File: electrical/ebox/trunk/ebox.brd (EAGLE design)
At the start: 100 x 80 mm, 162 parts, among them IC1 MAX3221CUE, IC10 SN74LVC1G125, IC11 MAX3221CUE, IC12 INA170, IC13 SN74LVC1G125, IC14 SN74LVC1G125, IC15 MAX3221CUE, IC17 SN74LVC1G125, IC18 SN74LVC1G125, IC19 74ALS04D, IC2 LT3652, IC20 AP1509-33, IC24 AP1509-5, IC3 XMEGA128A1, IC4 LT1161, IC5 SN74LVC1G125, IC6 SN74LVC1G125, IC7 MAX3221CUE, IC8 INA170, IC9 SN74LVC1G125, Q1 FDD4141TO252, U1 BLUETOOTH-RN42, U2 D2523T_, X1 BULLET, X10 DEANS, X11 DEANS, X12 7381-2PG-300, X13 B4B-ZR, X14 BULLET, X17 22-23-2021, X18 7381-3PG-300, X19 7381-3PG-300, X2 BULLET, X20 BULLET, X21 BULLET, X22 BULLET, X23 BULLET, X24 B4B-ZR, X3 17984-7PG-300, X4 BULLET, X5 17984-7PG-300, X6 17984-7PG-300, X7 17984-7PG-300, X8 22-23-2031, X9 22-23-2031

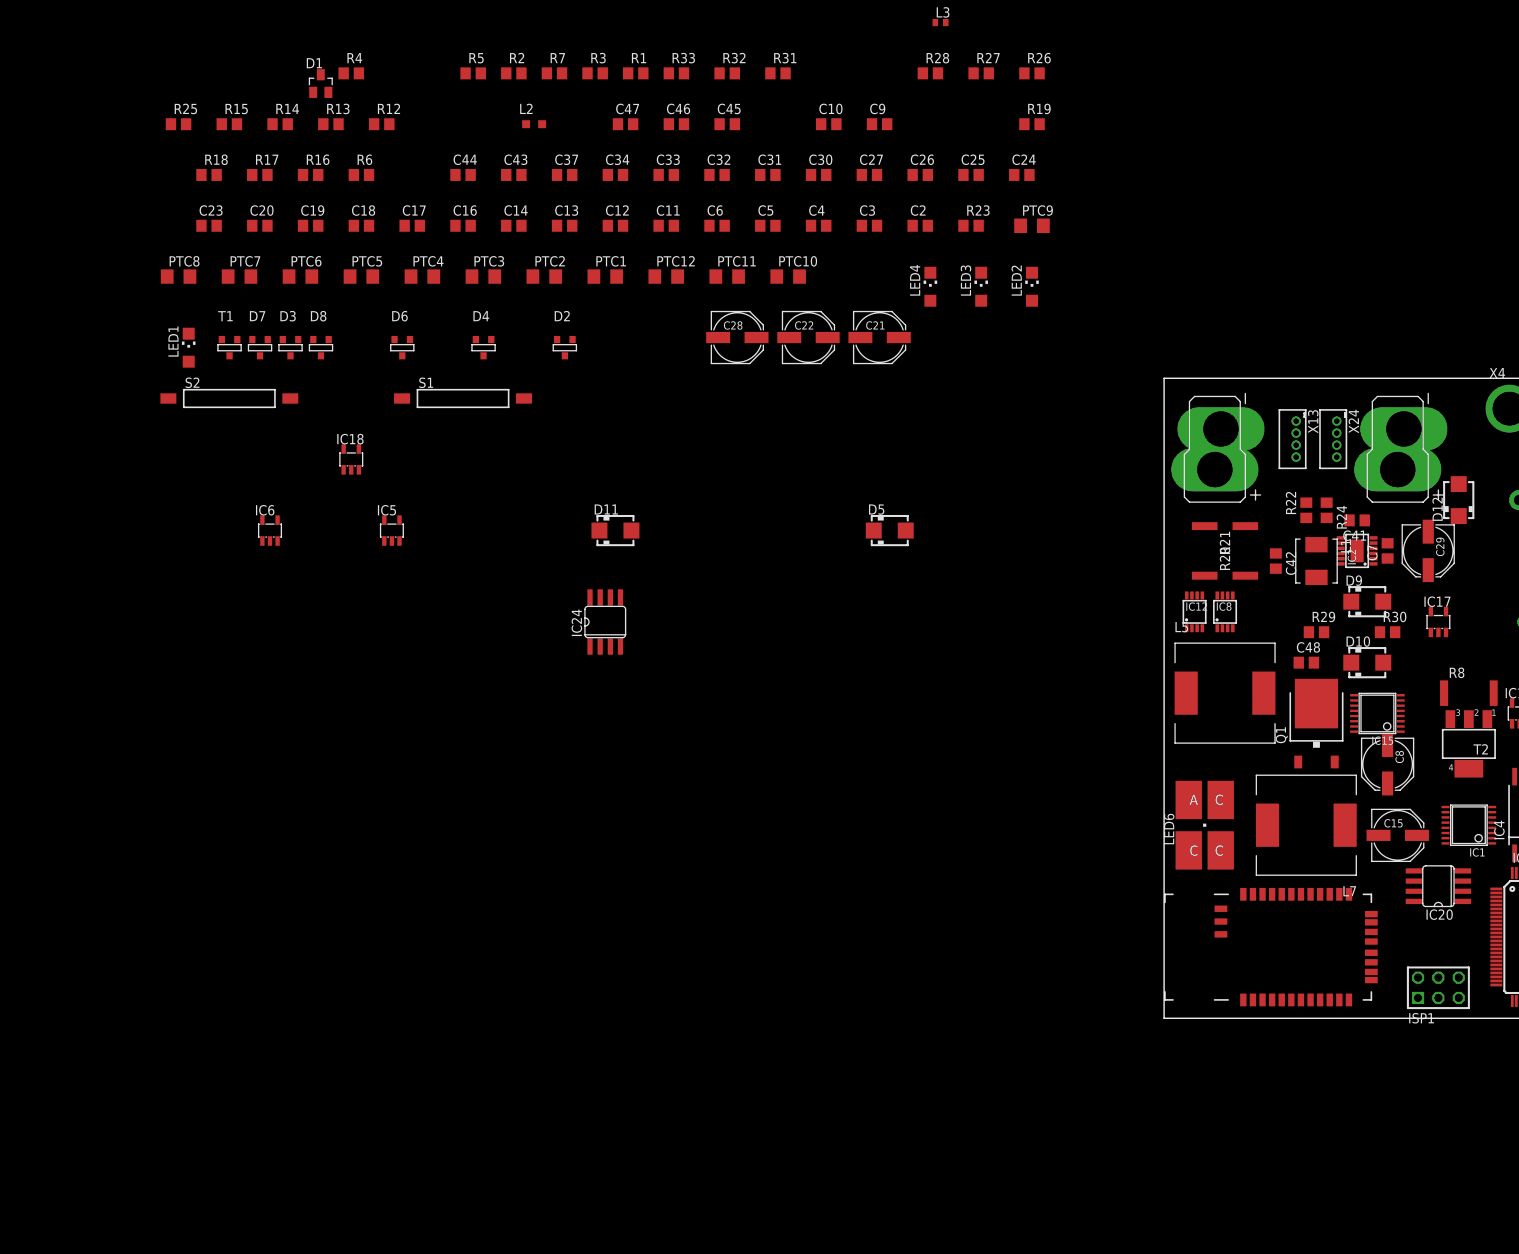
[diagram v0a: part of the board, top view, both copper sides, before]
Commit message: Removed switching regulators, replaced with onboard ESC BEC power.
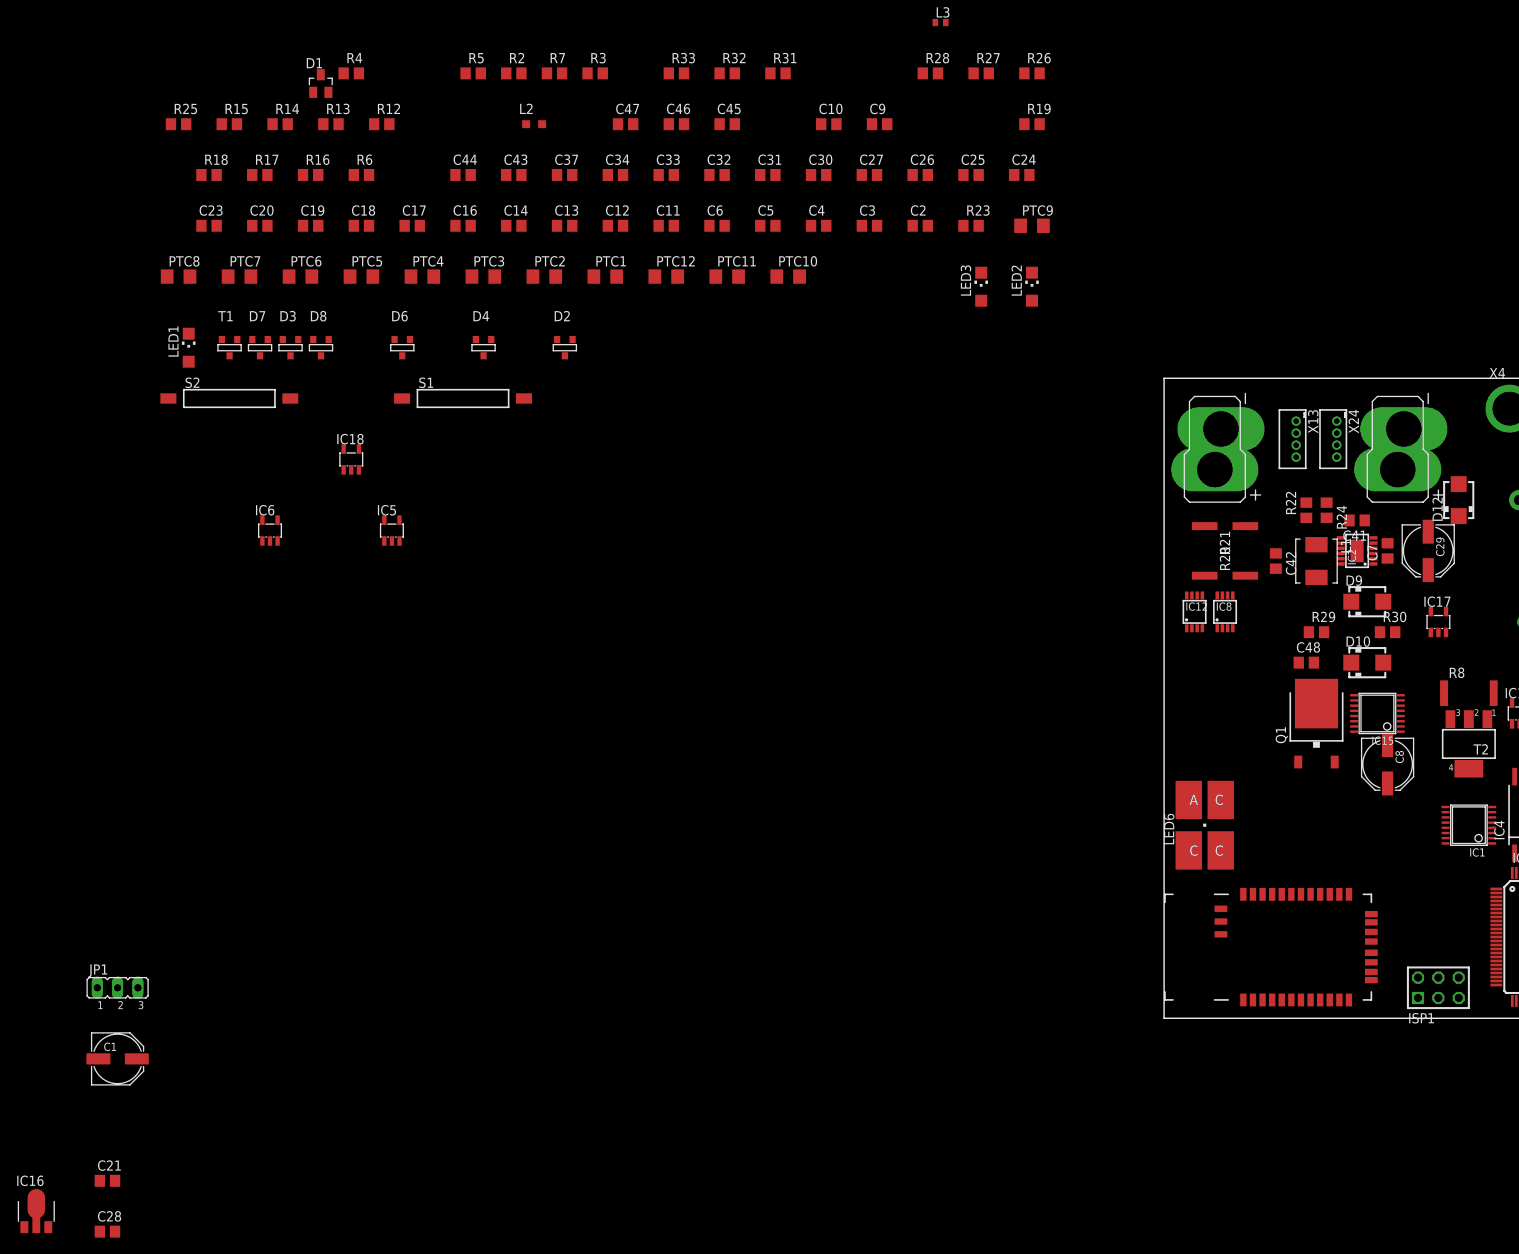
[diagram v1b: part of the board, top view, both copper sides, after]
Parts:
- removed C15: 68uF, rcl:PANASONIC_D
- removed C22: 220uF, rcl:PANASONIC_D
- removed D11, D5: MBRA340T3, diode:SMA
- removed IC20: AP1509-33, crw:SO08
- removed IC24: AP1509-5, crw:SO08
- removed L5, L7: 47uH, crw:SRR1280
- removed LED4: RED, led:CHIPLED_1206
- removed R1: 330, rcl:R0805
- added C1: 68uF, rcl:PANASONIC_D
- added IC16: MCP170333MB, linear:SOT89
- added JP1: (no value), jumper:JP2
- C21: value 68uF -> 1uF; device rcl:PANASONIC_D -> rcl:C0805
- C28: value 220uF -> 1uF; device rcl:PANASONIC_D -> rcl:C0805
- moved C21 142.9 mm to (-132.1, -20.3)
- moved C28 136.7 mm to (-132.1, -26.7)
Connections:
- removed net N$40: D5.C, IC20.2, L7.1
- removed net N$45: D11.C, IC24.2, L5.1
- removed net N$46: LED4.A, R1.1
- new net MOT1_5V: JP1.3, X8.2
- new net MOT2_5V: JP1.1, X9.2
- net +12V: no longer C15.+, C21.+, IC20.1, IC24.1
- net +3V3: now also C28.1, IC16.3; no longer C22.+, IC20.3, L7.2, R1.2
- net +5V: now also C1.+, C21.1, IC16.2@1, JP1.2; no longer C28.+, IC24.3, L5.2
- net GND: now also C1.-, C21.2, C28.2, IC16.1; no longer C15.-, C21.-, C22.-, C28.-, D11.A, D5.A, IC20.4, IC20.5, IC20.6, IC20.7, IC20.8, IC24.4, IC24.5, IC24.6, IC24.7, IC24.8, LED4.C

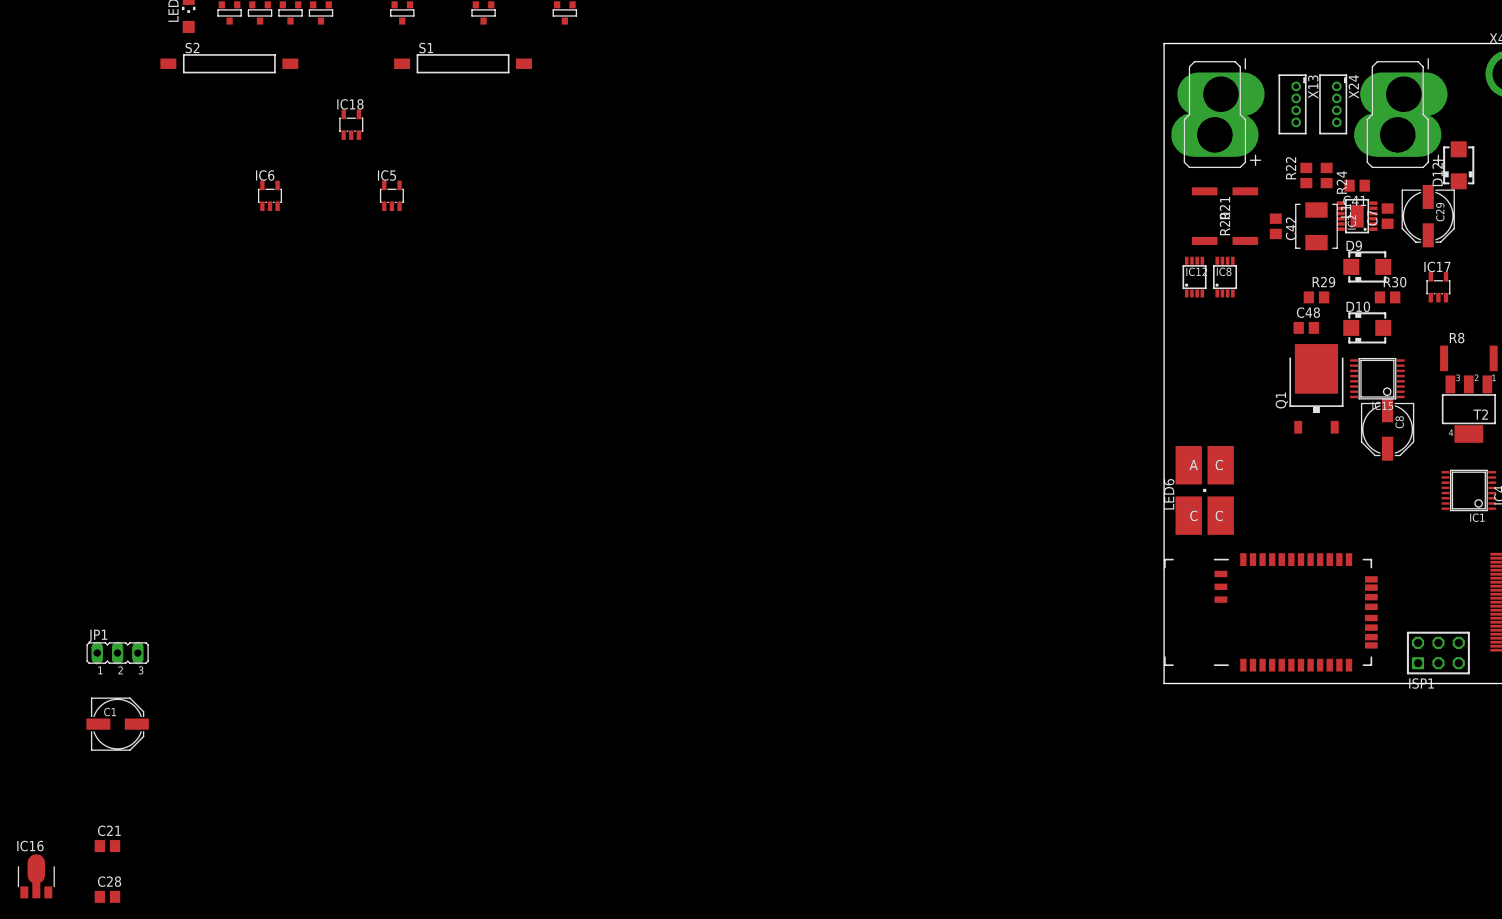
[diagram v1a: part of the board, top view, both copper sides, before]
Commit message: Added missing battery connectors for ESC.
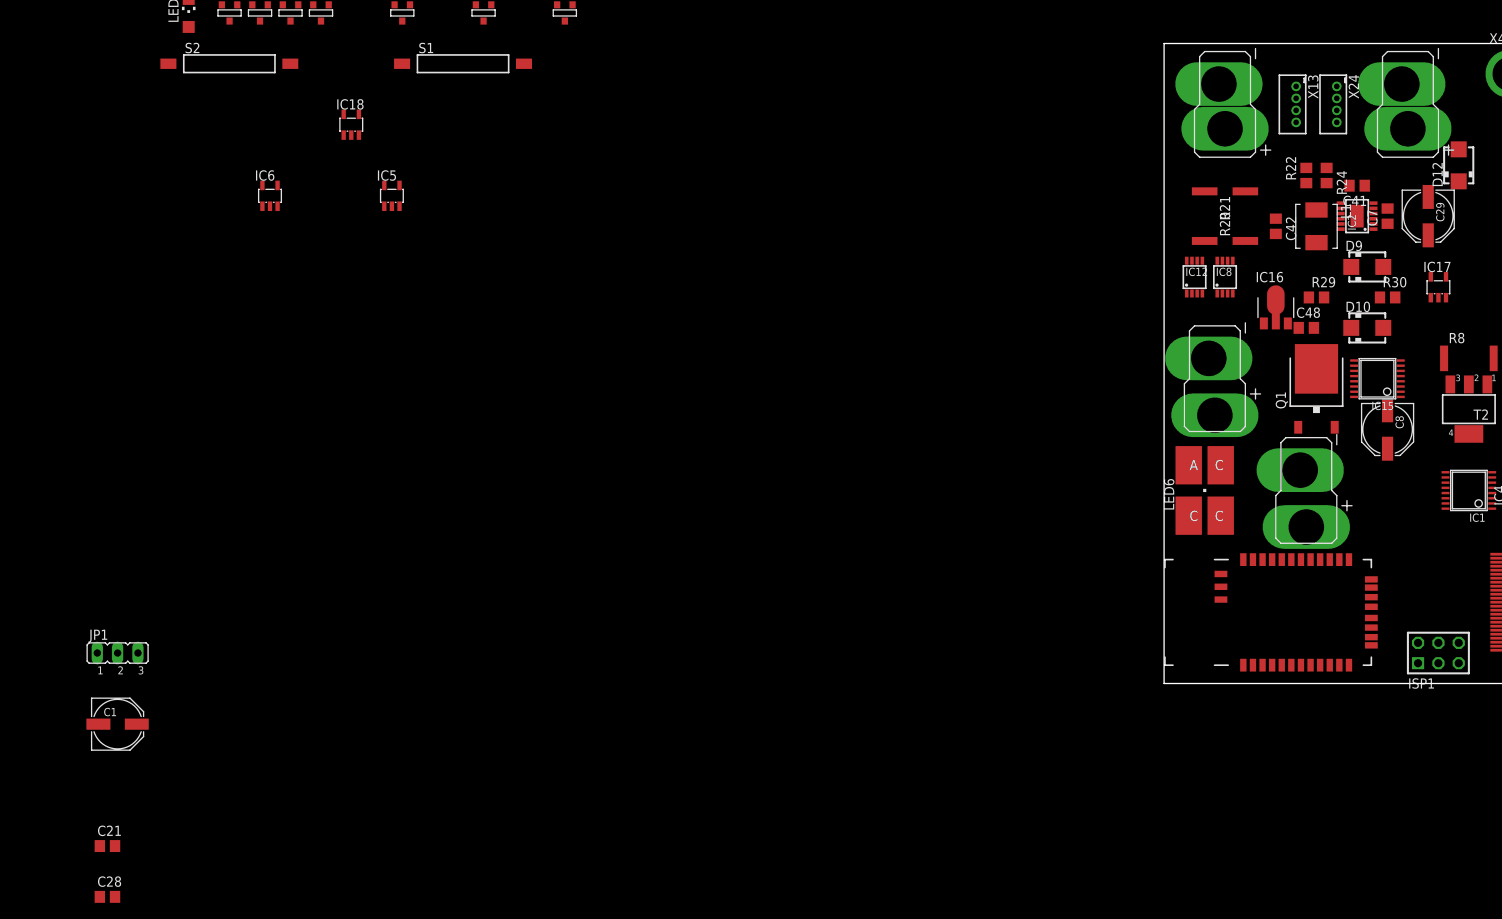
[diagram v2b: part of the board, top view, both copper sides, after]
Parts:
- added X15, X16: DEANS-FEMALE, crw:DEANS_FEMALE
- X10, X11: value DEANS -> DEANS-MALE; device crw:DEANS -> crw:DEANS_MALE
- moved IC16 170.5 mm to (14.0, 47.0)
- moved X10 1.80 mm to (7.62, 72.4)
- moved X11 1.80 mm to (30.5, 72.4)
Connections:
- net +12V: now also X15.POS, X16.POS
- net GND: now also X15.NEG, X16.NEG
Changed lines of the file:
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@@
 <element name="R32" library="rcl" package="R0805" value="330" x="-54.61" y="118.11"/>
 <element name="R33" library="rcl" package="R0805" value="330" x="-60.96" y="118.11"/>
-<element name="X10" library="crw" package="DEANS" value="DEANS" x="6.35" y="71.12"/>
-<element name="X11" library="crw" package="DEANS" value="DEANS" x="29.21" y="71.12"/>
 <element name="X12" library="crw" package="7381-2PG-300" value="7381-2PG-300" x="46.99" y="64.77" rot="MR0"/>
 <element name="X3" library="crw" package="17984-7PG-300" value="17984-7PG-300" x="46.99" y="49.53" rot="MR0"/>
@@
 <element name="C21" library="rcl" package="C0805" value="1uF" x="-132.08" y="-20.32"/>
 <element name="C28" library="rcl" package="C0805" value="1uF" x="-132.08" y="-26.67"/>
-<element name="IC16" library="linear" package="SOT89" value="MCP170333MB" x="-140.97" y="-24.13"/>
+<element name="IC16" library="linear" package="SOT89" value="MCP170333MB" x="13.97" y="46.99"/>
+<element name="X15" library="crw" package="DEANS_FEMALE" value="DEANS-FEMALE" x="6.35" y="38.1"/>
+<element name="X16" library="crw" package="DEANS_FEMALE" value="DEANS-FEMALE" x="17.78" y="24.13"/>
+<element name="X10" library="crw" package="DEANS_MALE" value="DEANS-MALE" x="7.62" y="72.39"/>
+<element name="X11" library="crw" package="DEANS_MALE" value="DEANS-MALE" x="30.48" y="72.39"/>
 </elements>
 <signals>
@@
 <contactref element="C21" pad="2"/>
 <contactref element="IC16" pad="1"/>
-<wire x1="-131.13" y1="-26.67" x2="-142.469" y2="-26.111" width="0" layer="19" extent="1-1"/>
+<contactref element="X15" pad="NEG"/>
+<contactref element="X16" pad="NEG"/>
+<wire x1="5.588" y1="40.64" x2="17.018" y2="26.67" width="0" layer="19" extent="1-1"/>
+<wire x1="12.471" y1="45.009" x2="5.588" y2="40.64" width="0" layer="19" extent="1-1"/>
+<wire x1="-131.13" y1="-26.67" x2="12.471" y2="45.009" width="0" layer="19" extent="1-1"/>
 <wire x1="-131.13" y1="-20.32" x2="-131.13" y2="-26.67" width="0" layer="19" extent="1-1"/>
 <wire x1="-133.21" y1="-5.08" x2="-131.13" y2="-20.32" width="0" layer="19" extent="1-1"/>
@@
 <contactref element="C28" pad="1"/>
 <contactref element="IC16" pad="3"/>
-<wire x1="-133.03" y1="-26.67" x2="-139.471" y2="-26.111" width="0" layer="19" extent="1-1"/>
+<wire x1="-133.03" y1="-26.67" x2="15.469" y2="45.009" width="0" layer="19" extent="1-1"/>
 <wire x1="-112.71" y1="62.26" x2="-133.03" y2="-26.67" width="0" layer="19" extent="1-1"/>
 <wire x1="-102.55" y1="71.15" x2="-112.71" y2="62.26" width="0" layer="19" extent="1-1"/>
@@
 <contactref element="R11" pad="2"/>
 <contactref element="C8" pad="+"/>
-<wire x1="71.68" y1="40.64" x2="85.8" y2="40.64" width="0" layer="19" extent="1-1"/>
-<wire x1="56.44" y1="40.64" x2="71.68" y2="40.64" width="0" layer="19" extent="1-1"/>
-<wire x1="55.245" y1="30.2" x2="56.44" y2="40.64" width="0" layer="19" extent="1-1"/>
-<wire x1="43.815" y1="30.2" x2="55.245" y2="30.2" width="0" layer="19" extent="1-1"/>
+<contactref element="X15" pad="POS"/>
+<contactref element="X16" pad="POS"/>
+<wire x1="6.35" y1="33.528" x2="17.78" y2="19.558" width="0" layer="19" extent="1-1"/>
+<wire x1="19.05" y1="39.33" x2="6.35" y2="33.528" width="0" layer="19" extent="1-1"/>
+<wire x1="27.94" y1="29.35" x2="19.05" y2="39.33" width="0" layer="19" extent="1-1"/>
+<wire x1="43.815" y1="30.2" x2="27.94" y2="29.35" width="0" layer="19" extent="1-1"/>
 <wire x1="41.2" y1="40.64" x2="43.815" y2="30.2" width="0" layer="19" extent="1-1"/>
-<wire x1="27.94" y1="29.35" x2="43.815" y2="30.2" width="0" layer="19" extent="1-1"/>
-<wire x1="19.05" y1="39.33" x2="27.94" y2="29.35" width="0" layer="19" extent="1-1"/>
+<wire x1="55.245" y1="30.2" x2="43.815" y2="30.2" width="0" layer="19" extent="1-1"/>
+<wire x1="56.44" y1="40.64" x2="55.245" y2="30.2" width="0" layer="19" extent="1-1"/>
+<wire x1="71.68" y1="40.64" x2="56.44" y2="40.64" width="0" layer="19" extent="1-1"/>
+<wire x1="85.8" y1="40.64" x2="71.68" y2="40.64" width="0" layer="19" extent="1-1"/>
 </signal>
 <signal name="AVR_VCC">
@@
 <signal name="BATT+">
 <contactref element="X13" pad="4"/>
-<contactref element="X10" pad="POS"/>
 <contactref element="X24" pad="4"/>
-<contactref element="X11" pad="POS"/>
 <contactref element="R20" pad="2"/>
 <contactref element="R21" pad="1"/>
@@
 <contactref element="IC8" pad="1"/>
 <contactref element="IC12" pad="2"/>
-<wire x1="21.59" y1="70.14" x2="29.21" y2="68.58" width="0" layer="19" extent="1-1"/>
-<wire x1="16.51" y1="70.14" x2="21.59" y2="70.14" width="0" layer="19" extent="1-1"/>
-<wire x1="17.78" y1="64.45" x2="16.51" y2="70.14" width="0" layer="19" extent="1-1"/>
-<wire x1="10.16" y1="61.52" x2="17.78" y2="64.45" width="0" layer="19" extent="1-1"/>
-<wire x1="5.08" y1="61.52" x2="10.16" y2="61.52" width="0" layer="19" extent="1-1"/>
-<wire x1="6.35" y1="68.58" x2="5.08" y2="61.52" width="0" layer="19" extent="1-1"/>
+<contactref element="X10" pad="POS"/>
+<contactref element="X11" pad="POS"/>
+<wire x1="7.62" y1="69.342" x2="30.48" y2="69.342" width="0" layer="19" extent="1-1"/>
+<wire x1="3.485" y1="48.75" x2="7.62" y2="69.342" width="0" layer="19" extent="1-1"/>
+<wire x1="6.645" y1="48.75" x2="3.485" y2="48.75" width="0" layer="19" extent="1-1"/>
+<wire x1="5.08" y1="61.52" x2="3.485" y2="48.75" width="0" layer="19" extent="1-1"/>
+<wire x1="10.16" y1="61.52" x2="5.08" y2="61.52" width="0" layer="19" extent="1-1"/>
+<wire x1="17.78" y1="64.45" x2="10.16" y2="61.52" width="0" layer="19" extent="1-1"/>
+<wire x1="16.51" y1="70.14" x2="17.78" y2="64.45" width="0" layer="19" extent="1-1"/>
+<wire x1="21.59" y1="70.14" x2="16.51" y2="70.14" width="0" layer="19" extent="1-1"/>
 <wire x1="22.08" y1="58.745" x2="17.78" y2="64.45" width="0" layer="19" extent="1-1"/>
 <wire x1="20" y1="48.26" x2="22.08" y2="58.745" width="0" layer="19" extent="1-1"/>
-<wire x1="6.645" y1="48.75" x2="5.08" y2="61.52" width="0" layer="19" extent="1-1"/>
-<wire x1="3.485" y1="48.75" x2="6.645" y2="48.75" width="0" layer="19" extent="1-1"/>
 </signal>
 <signal name="BATT2">
@@
 <signal name="BATT-">
 <contactref element="X13" pad="1"/>
+<contactref element="X24" pad="1"/>
 <contactref element="X10" pad="NEG"/>
-<contactref element="X24" pad="1"/>
 <contactref element="X11" pad="NEG"/>
-<wire x1="21.59" y1="74.64" x2="29.972" y2="73.66" width="0" layer="19" extent="1-1"/>
-<wire x1="16.51" y1="74.64" x2="21.59" y2="74.64" width="0" layer="19" extent="1-1"/>
-<wire x1="7.112" y1="73.66" x2="16.51" y2="74.64" width="0" layer="19" extent="1-1"/>
+<wire x1="6.858" y1="74.93" x2="29.718" y2="74.93" width="0" layer="19" extent="1-1"/>
+<wire x1="16.51" y1="74.64" x2="6.858" y2="74.93" width="0" layer="19" extent="1-1"/>
+<wire x1="21.59" y1="74.64" x2="16.51" y2="74.64" width="0" layer="19" extent="1-1"/>
 </signal>
 <signal name="MOT1_SIG">
@@
 <contactref element="C21" pad="1"/>
 <contactref element="IC16" pad="2@1"/>
-<wire x1="-133.03" y1="-20.32" x2="-140.97" y2="-23.19" width="0" layer="19" extent="1-1"/>
+<wire x1="-133.03" y1="-20.32" x2="13.97" y2="47.93" width="0" layer="19" extent="1-1"/>
 <wire x1="-128.41" y1="-5.08" x2="-133.03" y2="-20.32" width="0" layer="19" extent="1-1"/>
 <wire x1="-130.81" y1="3.81" x2="-128.41" y2="-5.08" width="0" layer="19" extent="1-1"/>
